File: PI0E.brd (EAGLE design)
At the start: 38 parts, among them T1 WE-LAN-10/100/1000-BASE-T,749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, X1 22-23-2021, X2 22-23-2021

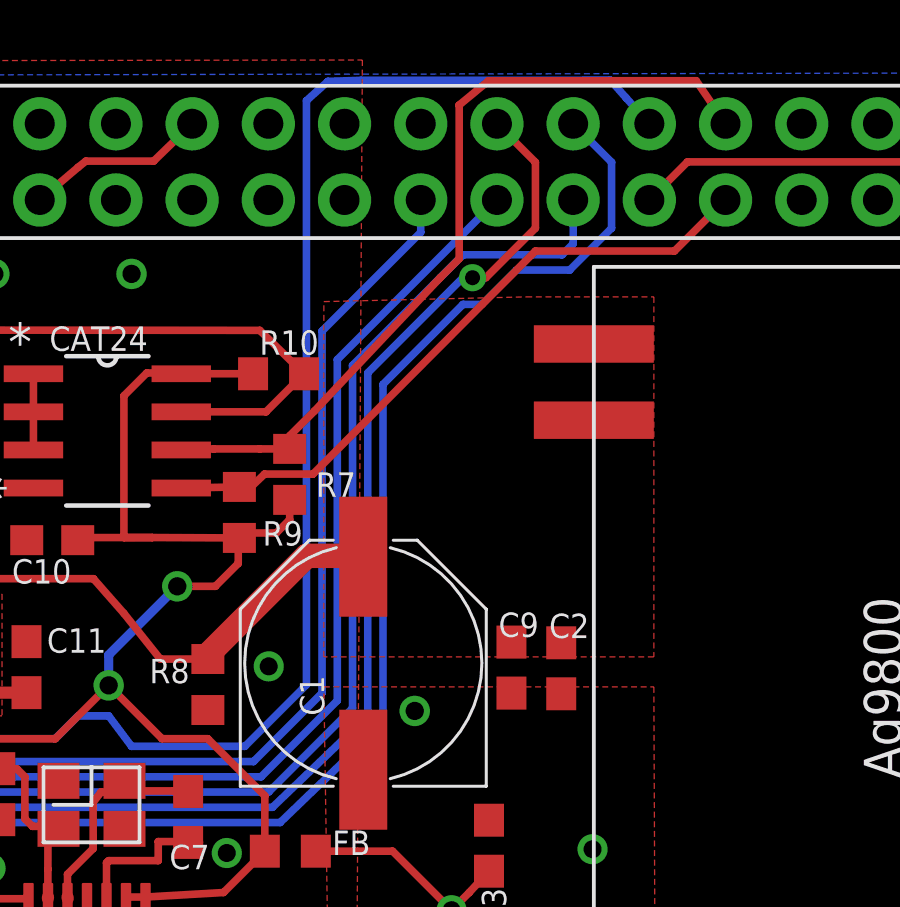
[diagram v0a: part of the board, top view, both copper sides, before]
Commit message: Improved wire appearence
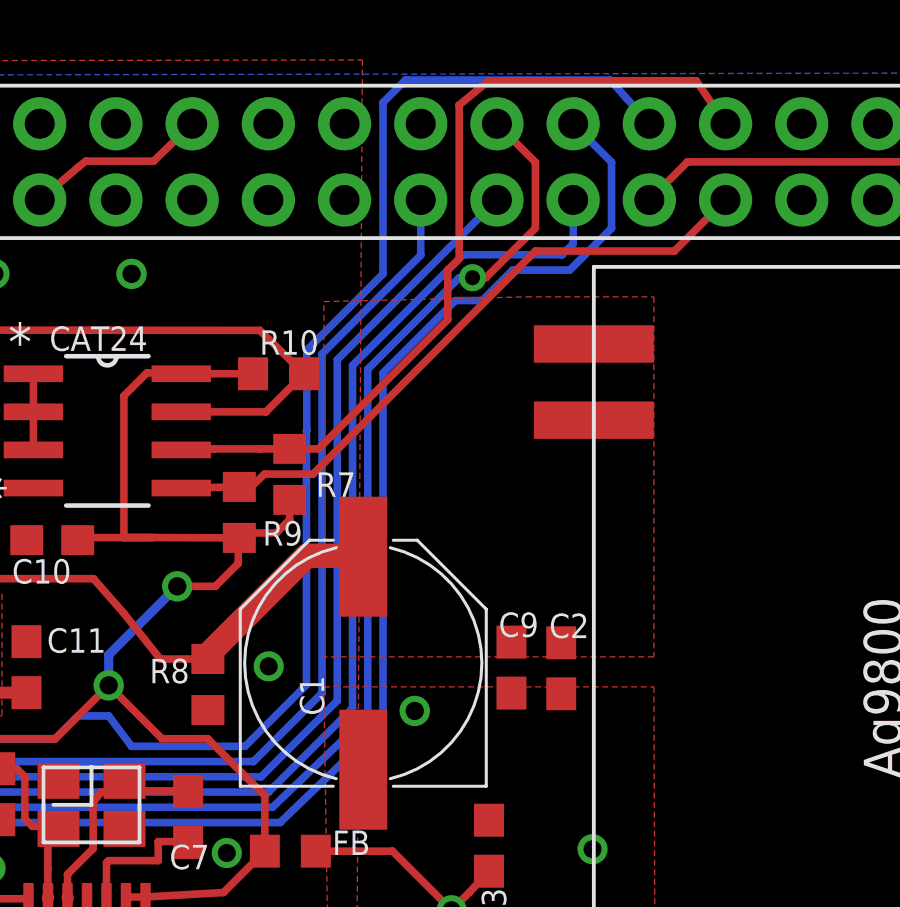
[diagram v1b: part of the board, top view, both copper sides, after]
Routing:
- net !CS2: track 60.4 -> 58.9 mm
- net ID_SC: track 27.3 -> 27.9 mm
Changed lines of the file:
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@@
 <wire x1="14.377" y1="3.836" x2="12.673" y2="3.836" width="0.254" layer="1"/>
 <wire x1="12.673" y1="3.836" x2="11.938" y2="4.571" width="0.254" layer="1"/>
-<wire x1="31.23" y1="35.23" x2="31.23" y2="34.151" width="0.254" layer="16"/>
-<wire x1="31.23" y1="34.151" x2="27.94" y2="30.861" width="0.254" layer="16"/>
-<wire x1="27.94" y1="30.861" x2="27.94" y2="18.796" width="0.254" layer="16"/>
+<wire x1="31.23" y1="35.23" x2="31.23" y2="33.389" width="0.254" layer="16"/>
+<wire x1="31.23" y1="33.389" x2="27.94" y2="30.099" width="0.254" layer="16"/>
+<wire x1="27.94" y1="30.099" x2="27.94" y2="18.796" width="0.254" layer="16"/>
 <wire x1="27.94" y1="18.796" x2="25.654" y2="16.51" width="0.254" layer="16"/>
 <wire x1="25.654" y1="16.51" x2="15.24" y2="16.51" width="0.254" layer="16"/>
@@
 <wire x1="37.592" y1="36.488" x2="37.592" y2="34.29" width="0.254" layer="16"/>
 <wire x1="37.592" y1="34.29" x2="36.195" y2="32.893" width="0.254" layer="16"/>
-<wire x1="36.195" y1="32.893" x2="34.417" y2="32.893" width="0.254" layer="16"/>
-<wire x1="34.417" y1="32.893" x2="33.274" y2="31.75" width="0.254" layer="16"/>
-<wire x1="33.274" y1="31.75" x2="32.639" y2="31.75" width="0.254" layer="16"/>
-<wire x1="32.639" y1="31.75" x2="29.972" y2="29.083" width="0.254" layer="16"/>
-<wire x1="29.972" y1="29.083" x2="29.972" y2="17.78" width="0.254" layer="16"/>
+<wire x1="36.195" y1="32.893" x2="34.29" y2="32.893" width="0.254" layer="16"/>
+<wire x1="34.29" y1="32.893" x2="33.274" y2="31.877" width="0.254" layer="16"/>
+<wire x1="33.274" y1="31.877" x2="32.385" y2="31.877" width="0.254" layer="16"/>
+<wire x1="32.385" y1="31.877" x2="29.972" y2="29.464" width="0.254" layer="16"/>
+<wire x1="29.972" y1="29.464" x2="29.972" y2="17.78" width="0.254" layer="16"/>
 <wire x1="29.972" y1="17.78" x2="26.543" y2="14.478" width="0.254" layer="16"/>
 <wire x1="26.543" y1="14.478" x2="16.256" y2="14.478" width="0.254" layer="16"/>
@@
 <wire x1="10.403" y1="11.166" x2="11.212" y2="11.178" width="0.254" layer="1"/>
 <via x="11.212" y="11.178" extent="1-16" drill="0.6096"/>
-<wire x1="27.42" y1="38.541" x2="28.137" y2="39.185" width="0.254" layer="16"/>
-<wire x1="28.137" y1="39.185" x2="29.242" y2="39.218" width="0.254" layer="16"/>
-<wire x1="29.242" y1="39.218" x2="37.549" y2="39.226" width="0.254" layer="16"/>
 <wire x1="37.549" y1="39.226" x2="38.073" y2="38.636" width="0.254" layer="16"/>
 <wire x1="38.073" y1="38.636" x2="38.85" y2="37.77" width="0.254" layer="16"/>
@@
 <wire x1="21.59" y1="17.018" x2="25.368" y2="17.018" width="0.254" layer="16"/>
 <wire x1="25.368" y1="17.018" x2="27.42" y2="19.07" width="0.254" layer="16"/>
-<wire x1="27.42" y1="38.541" x2="27.42" y2="19.07" width="0.254" layer="16"/>
+<wire x1="37.549" y1="39.226" x2="30.717" y2="39.226" width="0.254" layer="16"/>
+<wire x1="30.717" y1="39.226" x2="29.972" y2="38.481" width="0.254" layer="16"/>
+<wire x1="29.972" y1="38.481" x2="29.972" y2="32.766" width="0.254" layer="16"/>
+<wire x1="29.972" y1="32.766" x2="27.432" y2="30.226" width="0.254" layer="16"/>
+<wire x1="27.432" y1="30.226" x2="27.432" y2="27.559" width="0.254" layer="16"/>
+<wire x1="27.432" y1="27.559" x2="27.42" y2="27.547" width="0.254" layer="16"/>
+<wire x1="27.42" y1="27.547" x2="27.42" y2="19.07" width="0.254" layer="16"/>
 </signal>
 <signal name="ID_SD">
@@
 <wire x1="33.493" y1="39.205" x2="40.411" y2="39.205" width="0.254" layer="1"/>
 <wire x1="40.411" y1="39.205" x2="41.39" y2="37.77" width="0.254" layer="1"/>
-<wire x1="26.861" y1="26.933" x2="26.861" y2="27.369" width="0.254" layer="1"/>
-<wire x1="26.861" y1="27.369" x2="27.686" y2="28.194" width="0.254" layer="1"/>
+<wire x1="26.861" y1="26.933" x2="26.861" y2="27.369" width="0" layer="19" extent="1-16"/>
 <wire x1="32.512" y1="38.384" x2="32.506" y2="38.39" width="0.254" layer="1"/>
 <wire x1="32.512" y1="38.384" x2="32.512" y2="33.274" width="0.254" layer="1"/>
-<wire x1="32.512" y1="33.274" x2="31.877" y2="32.639" width="0.254" layer="1"/>
-<wire x1="31.877" y1="32.639" x2="27.686" y2="28.194" width="0.254" layer="1"/>
+<wire x1="32.512" y1="33.274" x2="32.131" y2="32.893" width="0.254" layer="1"/>
+<wire x1="32.131" y1="32.893" x2="32.131" y2="31.242" width="0.254" layer="1"/>
+<wire x1="32.131" y1="31.242" x2="27.822" y2="26.933" width="0.254" layer="1"/>
+<wire x1="27.822" y1="26.933" x2="26.861" y2="26.933" width="0.254" layer="1"/>
 </signal>
 <signal name="A0">
@@
 <wire x1="16.002" y1="14.986" x2="26.289" y2="14.986" width="0.254" layer="16"/>
 <wire x1="26.289" y1="14.986" x2="29.464" y2="18.034" width="0.254" layer="16"/>
-<wire x1="29.464" y1="18.034" x2="29.464" y2="29.464" width="0.254" layer="16"/>
-<wire x1="29.464" y1="29.464" x2="32.639" y2="32.639" width="0.254" layer="16"/>
-<wire x1="32.639" y1="32.639" x2="32.9565" y2="32.639" width="0.254" layer="16"/>
+<wire x1="29.464" y1="18.034" x2="29.464" y2="29.591" width="0.254" layer="16"/>
+<wire x1="29.464" y1="29.591" x2="32.512" y2="32.639" width="0.254" layer="16"/>
+<wire x1="32.512" y1="32.639" x2="32.9565" y2="32.639" width="0.254" layer="16"/>
 <via x="32.9565" y="32.639" extent="1-16" drill="0.5"/>
 <wire x1="32.9565" y1="32.639" x2="33.401" y2="32.639" width="0.254" layer="1"/>

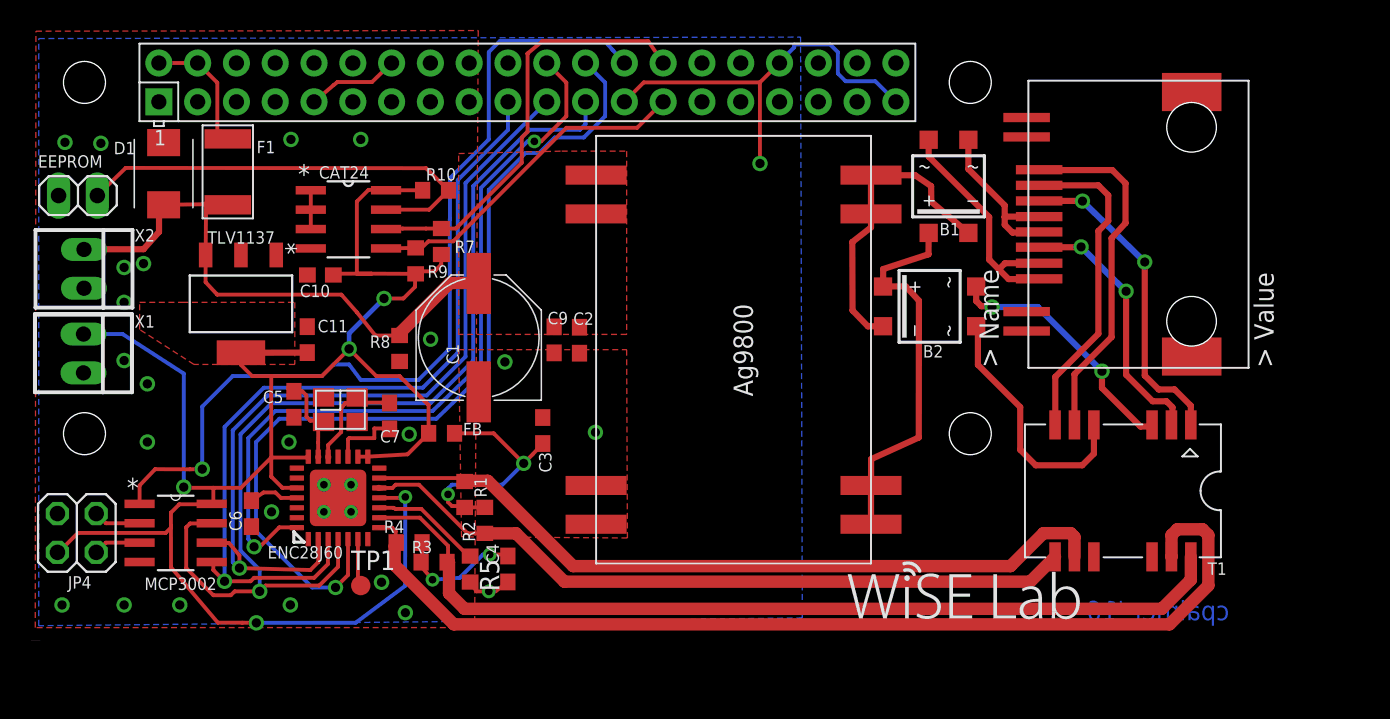
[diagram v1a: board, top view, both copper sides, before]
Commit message: Changed layout to match RPi 0 form factor more closely
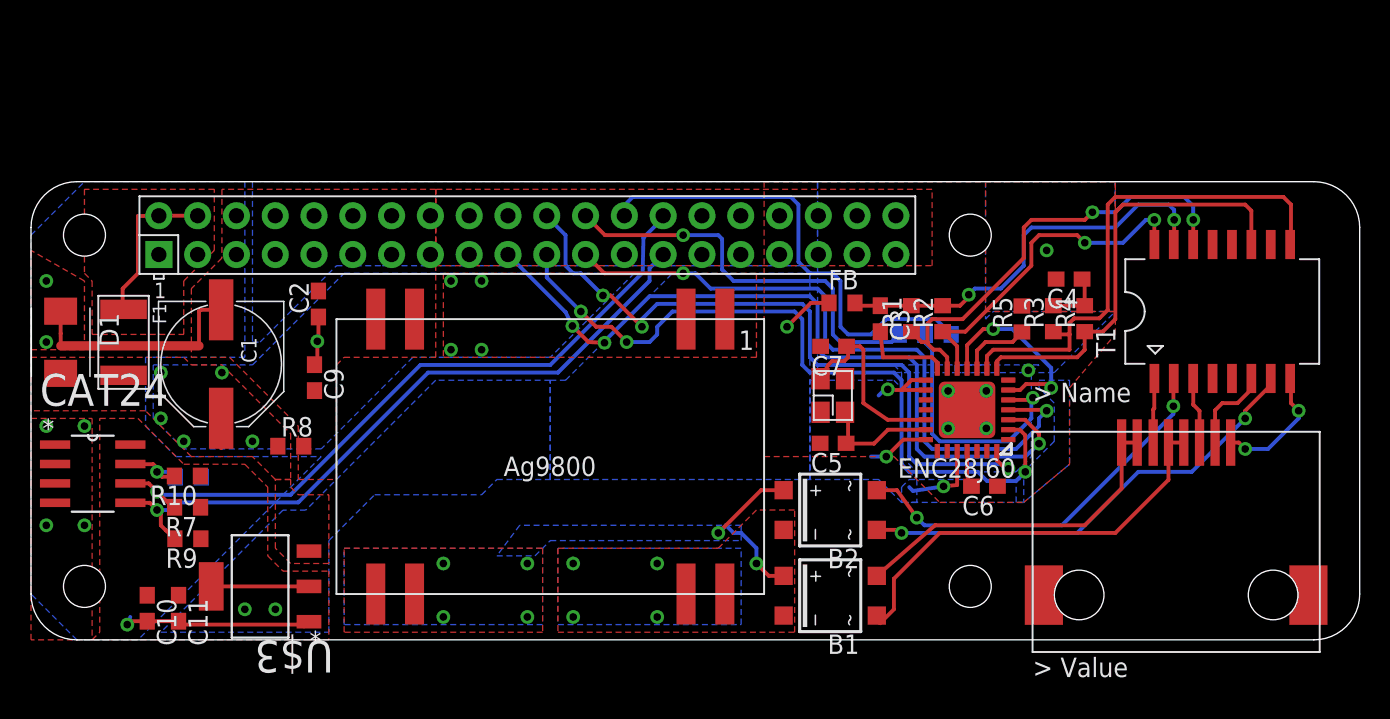
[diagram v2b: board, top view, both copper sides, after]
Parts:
- removed EEPROM: EEPROM, pinhead:1X02
- removed JP4: (no value), pinhead:2X02
- removed MCP3002: MCP3002-I/SN, Microchip_By_element14_Batch_1:SOIC127P600X175-8N
- removed TLV1137: TLV1117-33CDCY, Texas Instruments_By_element14_Batch_1:SOT230P700X180-4N
- removed TP1: TPB1,27, testpad:B1,27
- removed X1, X2: 22-23-2021, con-molex:22-23-2021
- added R11, R12, R6: 0, resistor:R0603
- added U$3: TLV1117TLV1117DCY, texas_instruments:SOT-223
- D1: value (none) -> 5V
- ENC28J60: value ENC28J60QFN28-ML_6X6MM -> (none)
- T1: value WE-LAN-10/100/1000-BASE-T,749020100 -> WE-LAN-10/100-BASE-T,749010011"; device EagleLibrary_Wuerth_Elektronik_eiSos_V4_20130318:749020100 -> EagleLibrary_Wuerth_Elektronik_eiSos_rev16a:749010011
- U$2: value AG9800M -> AG9800AG9800M; device ENC28J60-QFN:AG9800M -> silvertell:AG9800M
- U$4: value RJCSEX38X01X -> RJCSEX38X01XRJCSEX38X01X; device ENC28J60-QFN:RJCSEX38X01X -> rj45:RJCSEX38X01X
- moved C6 48.0 mm to (62.4, 10.1), turned to 180 degrees
- moved R4 46.6 mm to (69.0, 21.0), turned to 90 degrees
- moved R3 43.6 mm to (66.9, 21.0), turned to 90 degrees
- moved ENC28J60 41.6 mm to (61.3, 15.1), turned to 180 degrees
- moved C4 41.4 mm to (68.0, 23.6), turned to 180 degrees
- moved R5 39.7 mm to (64.9, 21.0), turned to 90 degrees
- moved C5 35.4 mm to (52.5, 12.9), turned to 180 degrees
- moved R2 32.8 mm to (59.7, 21.0)
- moved OSC 32.3 mm to (52.5, 16.0), turned to 90 degrees
- moved R1 31.4 mm to (57.6, 21.0), turned to 90 degrees
- moved C7 29.4 mm to (52.5, 19.2), turned to 180 degrees
- moved B1 27.9 mm to (52.3, 2.89), turned to 90 degrees
- moved FB 27.6 mm to (53.1, 22.1)
- moved R10 24.8 mm to (10.2, 10.7), turned to 180 degrees
- moved C10 24.6 mm to (7.61, 2.07), turned to 270 degrees
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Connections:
- removed net !CS: ENC28J60.5, U$1.24
- removed net !CS2: MCP3002.1, U$1.26
- removed net 1: T1.7, U$4.1
- removed net 2: T1.8, U$4.2
- removed net 3: T1.1, U$4.3
- removed net 6: T1.2, U$4.6
- removed net A0: JP4.1, MCP3002.2
- removed net A1: JP4.2, MCP3002.3
- removed net ARM_RTCK: U$1.31
- removed net ARM_TCK: U$1.33
- removed net ARM_TDI: U$1.7
- removed net ARM_TDO: U$1.29
- removed net ARM_TMS: U$1.32
- removed net I2CSCL: U$1.5
- removed net I2CSDA: U$1.3
- removed net N$13: C3.1, FB.2, R1.2, R2.2
- removed net N$40: ENC28J60.6, TP1.TP
- removed net N$9: B2.~1, T1.6
- new net !CE0: R6.1, U$1.24
- new net !CE1: R11.2, U$1.26
- new net !CEE: ENC28J60.5, R11.1, R6.2
- new net N$1: B2.~1, T1.7
- new net RD+: ENC28J60.9, R3.1, T1.9
- new net RD-: ENC28J60.8, R4.1, T1.11
- new net TCT: C3.1, FB.2, R1.2, R2.2, T1.15
- new net TD+: ENC28J60.13, R1.1, T1.14
- new net TD-: ENC28J60.12, R2.1, T1.16
- net +3V3: now also ENC28J60.6, U$3.P2, U$3.P4; no longer JP4.4, MCP3002.8, TLV1137.4, X1.1
- net +5V: now also U$2.P1, U$2.P2, U$3.P3; no longer TLV1137.3, U$2.+VDC1, U$2.+VDC2, X2.1
- net GND: now also R12.1, U$1.20, U$1.30, U$2.P3, U$3.P1; no longer EEPROM.1, JP4.3, MCP3002.4, TLV1137.1, U$2.-VDC, X1.2, X2.2
- net N$4: now also R12.2; no longer EEPROM.2
- net N$7: now also T1.2; no longer T1.3
- net RX+: now also T1.8, U$4.1; no longer ENC28J60.9, R3.1, T1.16
- net RX-: now also T1.6, U$4.2; no longer ENC28J60.8, R4.1, T1.15
- net SCK: no longer MCP3002.7
- net SI: no longer MCP3002.5
- net SO: no longer MCP3002.6
- net TX+: now also T1.3, U$4.3; no longer ENC28J60.13, R1.1, T1.10
- net TX-: now also T1.1, U$4.6; no longer ENC28J60.12, R2.1, T1.9
- net VIN+: now also U$2.P5, U$2.P6; no longer U$2.VIN+1, U$2.VIN+2
- net VIN-: now also U$2.P7, U$2.P8; no longer U$2.VIN-1, U$2.VIN-2
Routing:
- net +3V3: track 127.0 -> 37.5 mm, vias 5 -> 8
- net RX-: track 66.8 -> 5.76 mm
- net !CS2: track 58.9 -> 0.00 mm, vias 1 -> 0
- net !CS: track 58.6 -> 0.00 mm, vias 1 -> 0
- net RX+: track 59.9 -> 8.30 mm, vias 0 -> 2
- net TX+: track 50.3 -> 4.37 mm
- net TX-: track 47.9 -> 4.23 mm
- net RD+: track 0.00 -> 35.0 mm
- net +5V: track 37.8 -> 5.19 mm, vias 0 -> 10
- net N$1: track 0.00 -> 31.0 mm, vias 0 -> 2
- net !CE1: track 0.00 -> 30.8 mm
- net TD+: track 0.00 -> 30.8 mm, vias 0 -> 2
- net RD-: track 0.00 -> 28.6 mm
- net TCT: track 0.00 -> 28.3 mm, vias 0 -> 2
- net !CE0: track 0.00 -> 27.1 mm, vias 0 -> 1
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- added copper zone on layer 16, net +3V3
- added copper zone on layer 16, net +5V
- added copper zone on layer 1, net 5V0@1
- added copper zone on layer 1, net VIN+
- added copper zone on layer 16, net VIN+
- added copper zone on layer 1, net VIN-
- added copper zone on layer 16, net VIN-
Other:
- board outline added: 87 x 30 mm
- board text removed: "/Users/agr/Desktop/wise_logo_pcb.bmp"
- board text removed: "C Palmer"
- board text removed: "cpalmer '16"
